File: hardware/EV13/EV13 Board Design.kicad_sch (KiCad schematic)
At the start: 136 parts, among them CN2 Conn_05x02_Female, CN3 Conn_01x06_Female, CN4 Conn_01x06_Female, CN5 Conn_02x05_Male, CN6 Conn_02x05_Male, CN7 Conn_02x05_Male, J1 Conn_01x02_Socket, J10 Conn_01x08_Socket, J2 AudioJack1, J3 Conn_01x06_Socket, J9 USB_C_Receptacle, SW1 TS-1037-A11B3-D2, SW3 TS-1037-A11B3-D2, SW4 SW_Push, SW5 SW_Push, SW6 SW_SPDT, U1 STM32F405RGTx, U11 ESP32-S3-WROOM-1-N8R2, U13 BM14B(0.8)-24DS-0.4V(53), U2 BQ21040DBV, U3 CH340C, U4 USBLC6-2P6, U5 M24C02-RMN6TP, U6 WM8960CGEFL/RV, U7 TPS63060, U8 STM32F072CBTx, Y1 Crystal_GND24

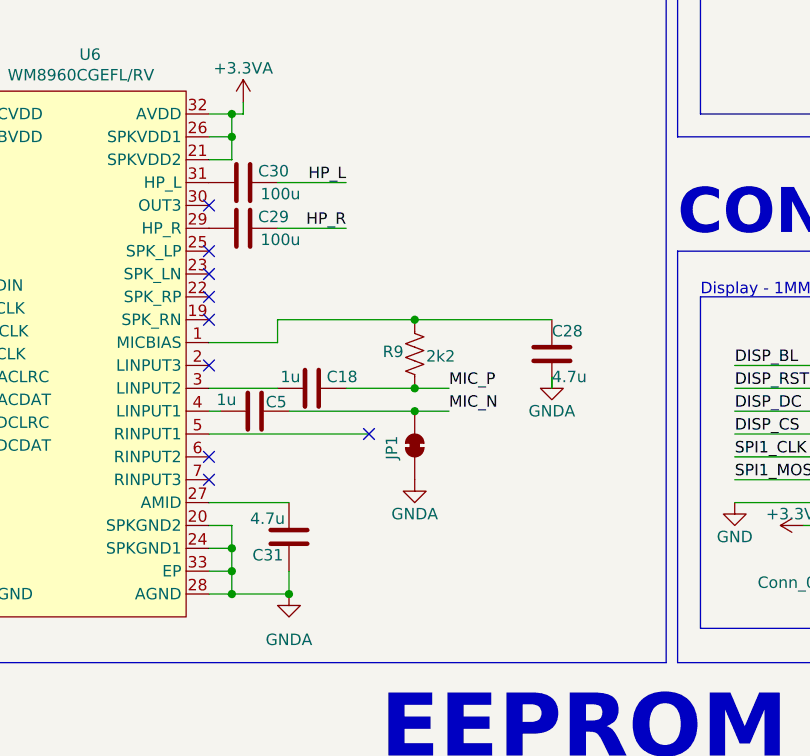
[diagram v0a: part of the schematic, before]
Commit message: chore: switch to smaller symbols so we have more space around the audio chip
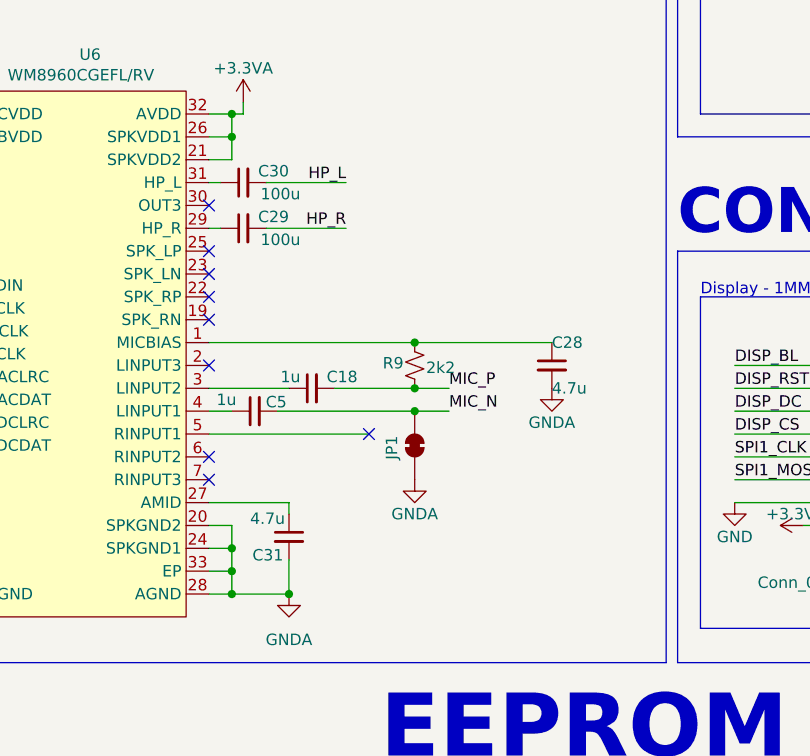
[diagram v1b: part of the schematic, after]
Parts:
- C18, C28, C29, C30, C31, C5: symbol Device:C -> Device:C_Small
- R9: symbol Device:R_US -> Device:R_Small_US
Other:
- moved on the sheet: C28

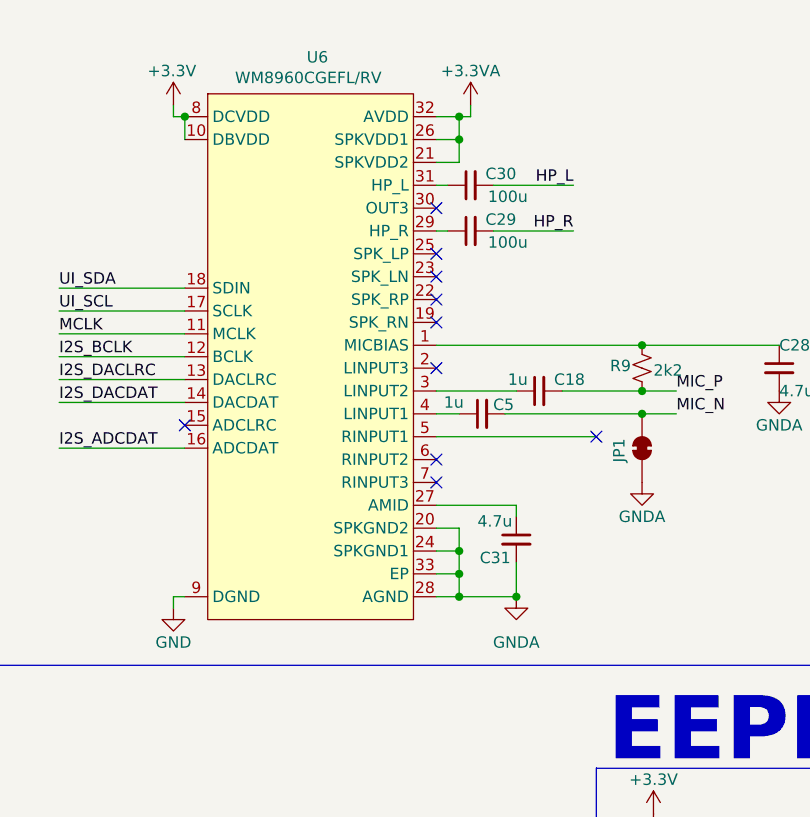
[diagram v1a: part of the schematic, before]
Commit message: chore: Put all unused audio inputs and outputs to GNDA
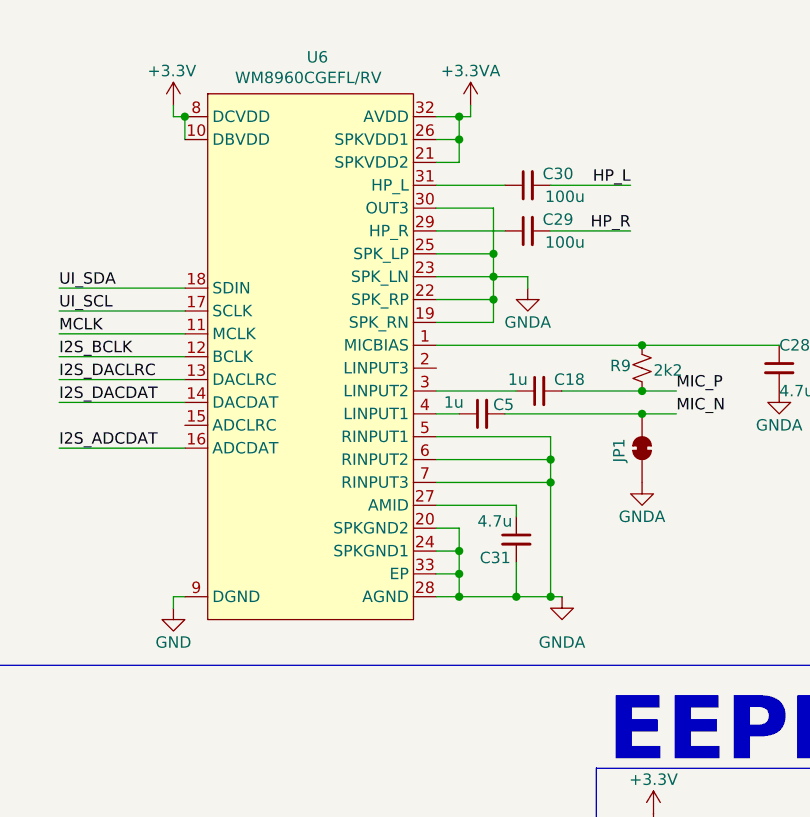
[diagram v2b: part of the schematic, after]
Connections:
- net GNDA: now also U6.19 (SPK_RN), U6.22 (SPK_RP), U6.23 (SPK_LN), U6.25 (SPK_LP), U6.30 (OUT3), U6.5 (RINPUT1), U6.6 (RINPUT2), U6.7 (RINPUT3)
- no-connect marks 46 -> 36
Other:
- moved on the sheet: C29, C30

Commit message: chore: Move usb_cc1/2_detect to mgmt from ui
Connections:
- net USB_CC1_DETECT: now also U8.4 (PC15); no longer U1.11 (PC3)
- net USB_CC2_DETECT: now also U8.3 (PC14); no longer U1.10 (PC2)
- no-connect marks 36 -> 34
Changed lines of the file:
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@@
 	)
 	(no_connect
-		(at 73.66 116.84)
-	)
-	(no_connect
 		(at 196.85 104.14)
 	)
@@
 	)
 	(no_connect
-		(at 73.66 114.3)
-	)
-	(no_connect
 		(at 340.36 274.32)
 	)
@@
 		)
 	)
+	(wire
+		(pts
+			(xy 55.88 116.84) (xy 73.66 116.84)
+		)
+		(stroke
+			(width 0)
+			(type default)
+		)
+	)
 	(polyline
 		(pts
@@
 	(wire
 		(pts
+			(xy 55.88 114.3) (xy 73.66 114.3)
+		)
+		(stroke
+			(width 0)
+			(type default)
+		)
+	)
+	(wire
+		(pts
 			(xy 485.14 240.03) (xy 468.63 240.03)
 		)
@@
 		)
 	)
+	(label "USB_CC1_DETECT"
+		(at 55.88 116.84 0)
+		(effects
+			(font
+				(size 1.27 1.27)
+			)
+			(justify left bottom)
+		)
+	)
 	(label "DISP_DC"
 		(at 314.96 226.06 0)
@@
 		)
 	)
-	(label "USB_CC2_DETECT"
-		(at 416.56 119.38 180)
-		(effects
-			(font
-				(size 1.27 1.27)
-			)
-			(justify right bottom)
-		)
-	)
 	(label "NET_STAT"
 		(at 242.57 111.76 180)
@@
 		)
 	)
+	(label "USB_CC2_DETECT"
+		(at 55.88 114.3 0)
+		(effects
+			(font
+				(size 1.27 1.27)
+			)
+			(justify left bottom)
+		)
+	)
 	(label "USB_RTS_MGMT"
 		(at 121.92 124.46 180)
@@
 		(effects
 			(font
-				(size 1.27 1.27)
-			)
-			(justify right bottom)
-		)
-	)
-	(label "USB_CC1_DETECT"
-		(at 416.56 121.92 180)
-		(effects
-			(font

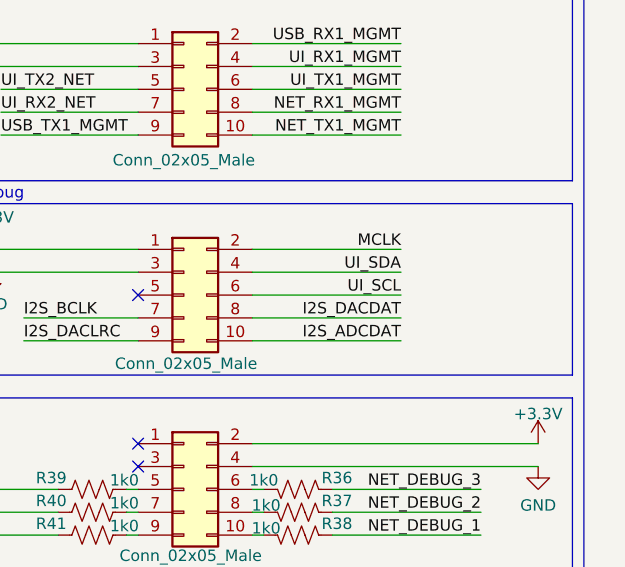
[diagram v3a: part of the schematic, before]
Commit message: chore: Add resistor to mco to gnd to reduce rf noise
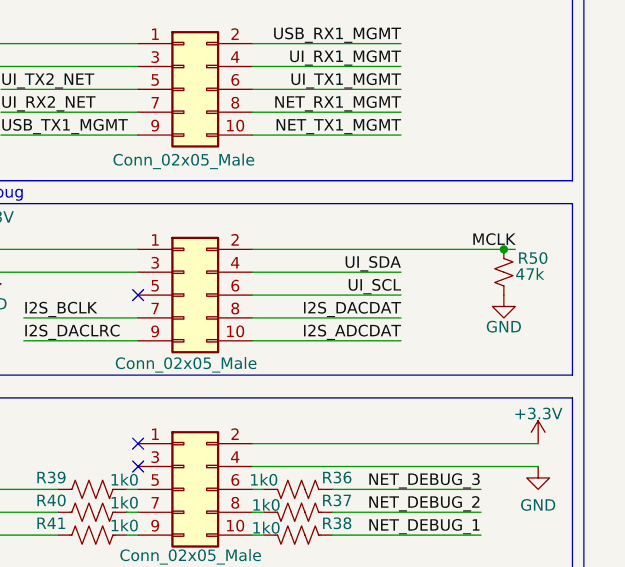
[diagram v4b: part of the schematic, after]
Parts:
- added R50: 47k, Resistor_SMD:R_0402_1005Metric, symbol Device:R_Small_US
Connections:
- net GND: now also R50.1
- net MCLK: now also R50.2
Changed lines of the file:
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@@
 	)
 	(junction
+		(at 496.57 240.03)
+		(diameter 0)
+		(color 0 0 0 0)
+	)
+	(junction
 		(at 71.12 370.84)
 		(diameter 0)
@@
 	(wire
 		(pts
-			(xy 485.14 240.03) (xy 468.63 240.03)
+			(xy 468.63 240.03) (xy 496.57 240.03)
 		)
 		(stroke
@@
 	(wire
 		(pts
+			(xy 497.84 240.03) (xy 496.57 240.03)
+		)
+		(stroke
+			(width 0)
+			(type default)
+		)
+	)
+	(wire
+		(pts
 			(xy 85.09 311.15) (xy 86.36 311.15)
 		)
@@
 	)
 	(label "MCLK"
-		(at 485.14 240.03 180)
+		(at 497.84 240.03 180)
 		(effects
 			(font
@@
 	)
 	(symbol
+		(lib_id "power:GND")
+		(at 496.57 245.11 0)
+		(mirror y)
+		(unit 1)
+		(exclude_from_sim no)
+		(in_bom yes)
+		(on_board yes)
+		(dnp no)
+		(property "Reference" "#PWR64"
+			(at 496.57 251.46 0)
+			(effects
+				(font
+					(size 1.27 1.27)
+				)
+				(hide yes)
+			)
+		)
+		(property "Value" "GND"
+			(at 496.57 248.666 0)
+			(effects
+				(font
+					(size 1.27 1.27)
+				)
+			)
+		)
+		(property "Footprint" ""
+			(at 496.57 245.11 0)
+			(effects
+				(font
+					(size 1.27 1.27)
+				)
+				(hide yes)
+			)
+		)
+		(property "Datasheet" ""
+			(at 496.57 245.11 0)
+			(effects
+				(font
+					(size 1.27 1.27)
+				)
+				(hide yes)
+			)
+		)
+		(property "Description" "Power symbol creates a global label with name \"GND\" , ground"
+			(at 496.57 245.11 0)
+			(effects
+				(font
+					(size 1.27 1.27)
+				)
+				(hide yes)
+			)
+		)
+		(pin "1"
+		)
+		(instances
+			(project "EV13 Board Design"
+				(path "/bd865368-262b-4f76-b7a6-1673c2cb0f8c"
+					(reference "#PWR64")
+					(unit 1)
+				)
+			)
+		)
+	)
+	(symbol
 		(lib_id "power:+3.3V")
 		(at 322.58 238.76 90)
@@
 					(unit 1)
 				)
+			)
+		)
+	)
+	(symbol
+		(lib_id "Device:R_Small_US")
+		(at 496.57 242.57 180)
+		(unit 1)
+		(exclude_from_sim no)
+		(in_bom yes)
+		(on_board yes)
+		(dnp no)
+		(property "Reference" "R50"
+			(at 498.094 241.046 0)
+			(effects
+				(font
+					(size 1.27 1.27)
+				)
+				(justify right)
+			)
+		)
+		(property "Value" "47k"
+			(at 497.84 242.824 0)
+			(effects
+				(font
+					(size 1.27 1.27)
+				)
+				(justify right)
+			)
+		)
+		(property "Footprint" "Resistor_SMD:R_0402_1005Metric"
+			(at 496.57 242.57 0)
+			(effects
+				(font
+					(size 1.27 1.27)
+				)
+				(hide yes)
+			)
+		)
+		(property "Datasheet" "~"
+			(at 496.57 242.57 0)
+			(effects
+				(font
+					(size 1.27 1.27)
+				)
+				(hide yes)
+			)
+		)
+		(property "Description" "Resistor, small US symbol"
+			(at 496.57 242.57 0)
+			(effects
+				(font
+					(size 1.27 1.27)
+				)
+				(hide yes)
+			)
+		)
+		(property "JLCPCB Part #" "C25879"
+			(at 496.57 242.57 0)
+			(effects
+				(font
+					(size 1.27 1.27)
+				)
+				(hide yes)
+			)
+		)
+		(pin "1"
+		)
+		(pin "2"
+		)
+		(instances
+			(project "EV13 Board Design"
+				(path "/bd865368-262b-4f76-b7a6-1673c2cb0f8c"
+					(reference "R50")
+					(unit 1)
+				)

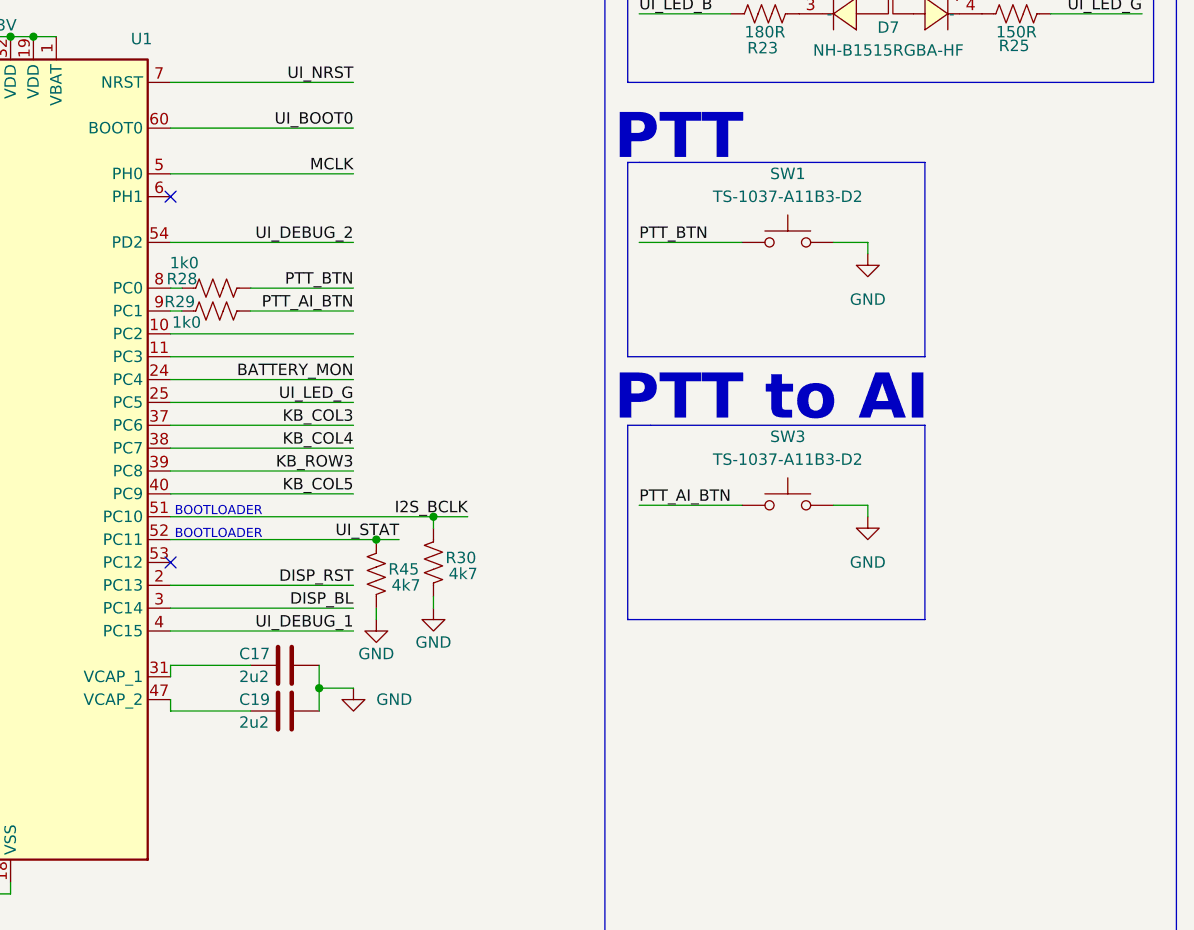
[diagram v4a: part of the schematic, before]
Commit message: feat: Adding debounce to ptt buttons WIP
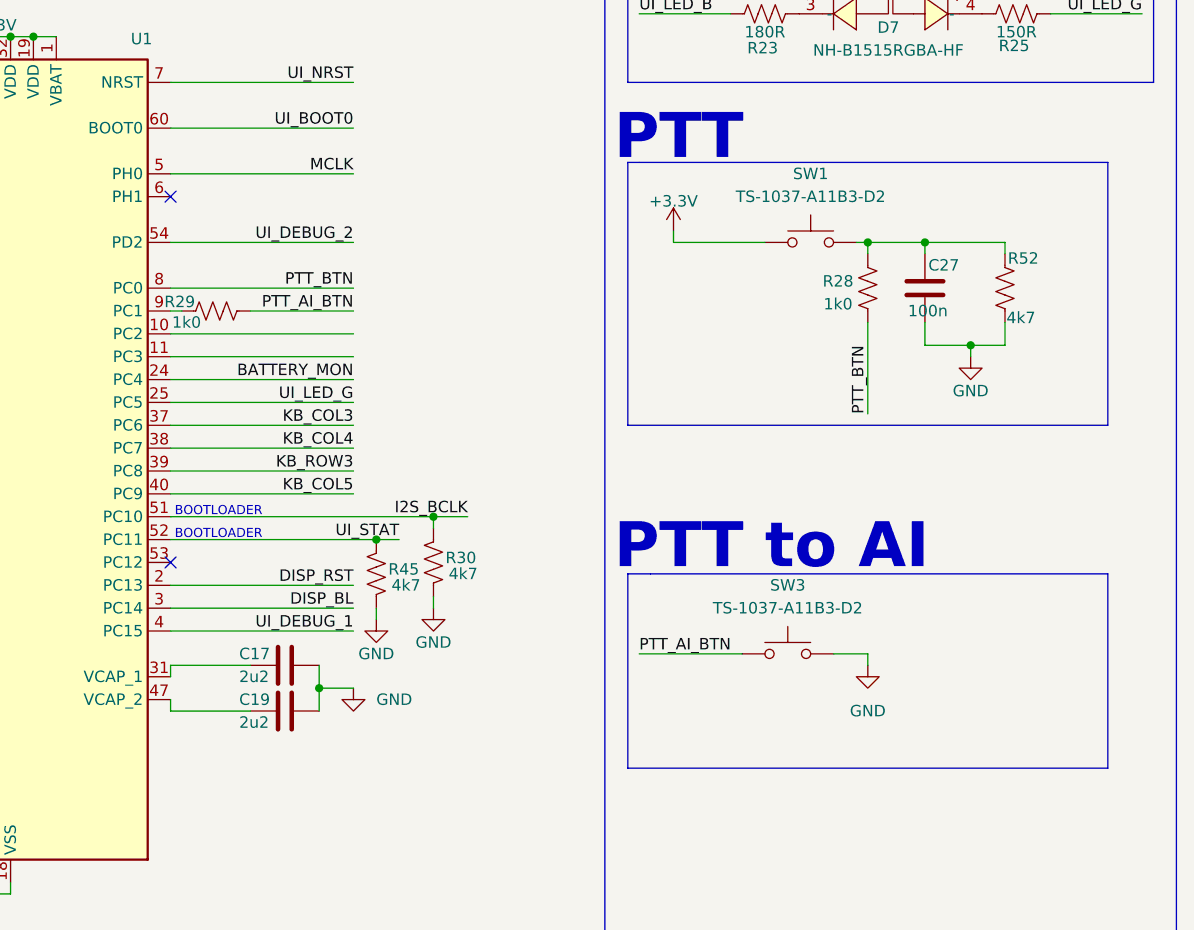
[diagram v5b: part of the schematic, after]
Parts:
- added C27: 100n, Capacitor_SMD:C_0402_1005Metric, symbol Device:C
- added R52: 4k7, Resistor_SMD:R_0402_1005Metric, symbol Device:R_US
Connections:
- net +3.3V: now also SW1.1
- net GND: now also C27.1, R52.1; no longer SW1.2
- net PTT_BTN: now also R28.1, U1.8 (PC0); no longer R28.2, SW1.1
- new net: C27.2, R28.2, R52.2, SW1.2
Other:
- moved on the sheet: R28, SW1, SW3

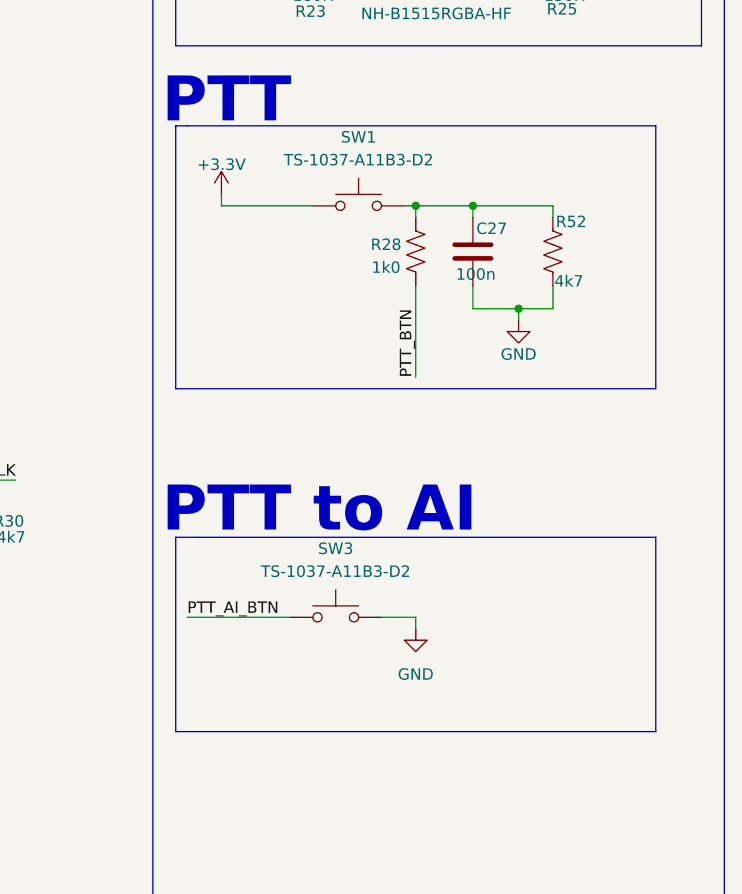
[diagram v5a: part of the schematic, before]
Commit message: feat: Add rc debounce circuits to ptt and ptt ai buttons
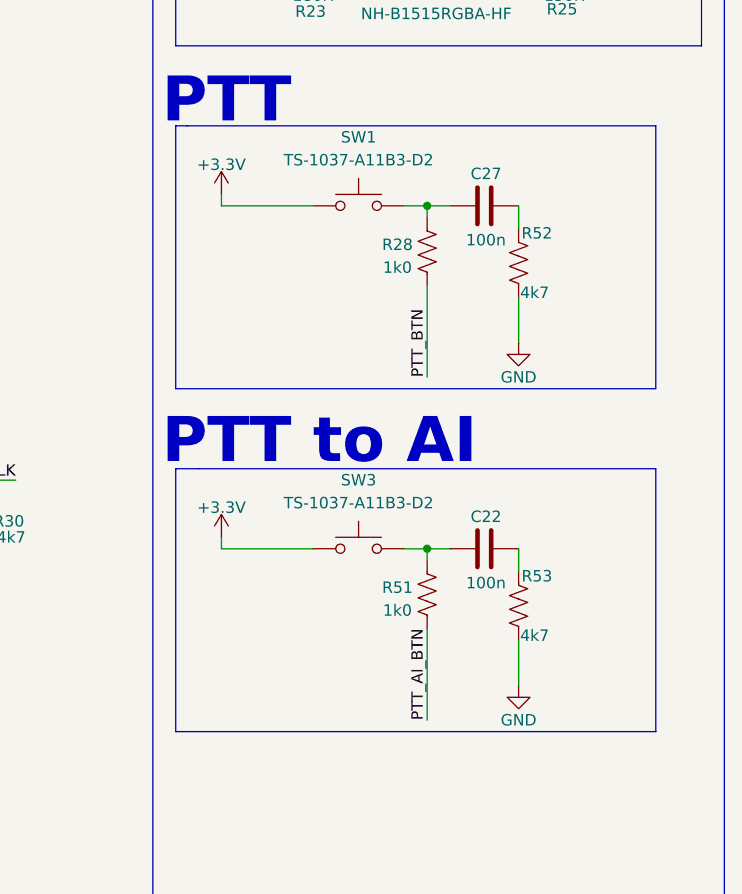
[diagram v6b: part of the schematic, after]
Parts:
- added C22: 100n, Capacitor_SMD:C_0402_1005Metric, symbol Device:C
- added R51: 1k0, Resistor_SMD:R_0402_1005Metric, symbol Device:R_US
- added R53: 4k7, Resistor_SMD:R_0402_1005Metric, symbol Device:R_US
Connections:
- net +3.3V: now also SW3.1
- net GND: now also R53.1; no longer C27.1, SW3.2
- net PTT_AI_BTN: now also R51.1; no longer SW3.1
- net at C27.2, R28.2, SW1.2: no longer R52.2
- new net: C22.2, R51.2, SW3.2
- new net: C22.1, R53.2
- new net: C27.1, R52.2
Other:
- moved on the sheet: C27, R28, R52, SW3
